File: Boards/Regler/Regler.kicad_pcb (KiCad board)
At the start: 2 copper layers, 160 x 50 mm, 6 parts, among them P1 LV_In, P2 LV_Out_L, P3 LV_Out_R

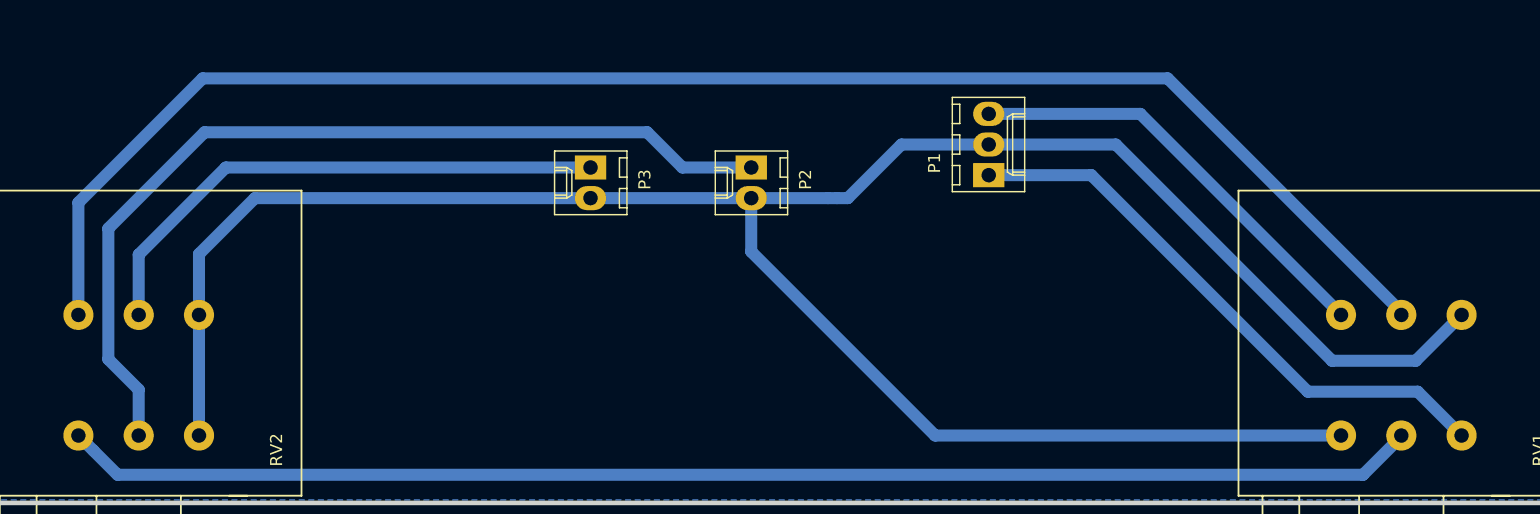
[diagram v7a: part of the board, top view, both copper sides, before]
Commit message: Added Test, moved mounting holes
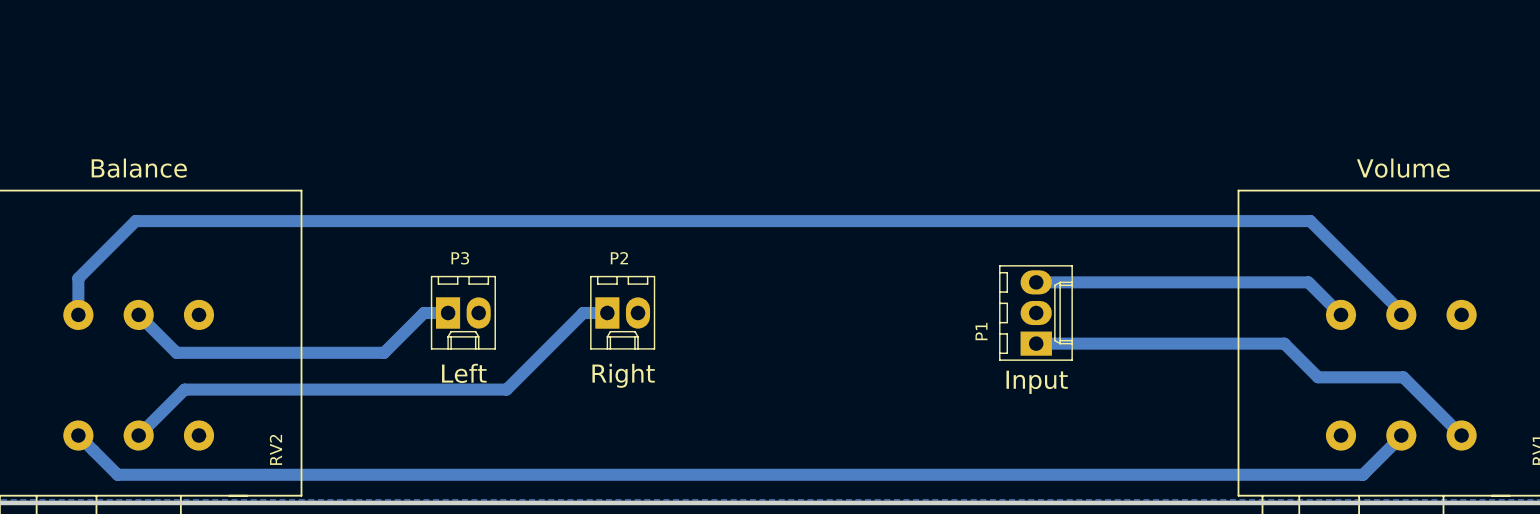
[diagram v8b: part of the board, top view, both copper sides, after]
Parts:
- moved P2 17.0 mm to (122.7, 121.9), turned to 0 degrees
- moved P3 16.9 mm to (109.5, 121.9), turned to 0 degrees
- moved P1 14.5 mm to (158.2, 124.5)
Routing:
- net Earth_Clean: track 192.2 -> 0.00 mm
- net Net-(P2-Pad1): track 76.0 -> 43.1 mm
- net Net-(P3-Pad1): track 45.5 -> 28.3 mm
- net Net-(RV1-Pad5): track 131.5 -> 118.1 mm
- net Net-(P1-Pad3): track 36.1 -> 26.4 mm
- net Net-(P1-Pad1): track 48.2 -> 38.4 mm
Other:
- board text added: "Balance"
- board text added: "Input"
- board text added: "Left"
- board text added: "Right"
- board text added: "Volume"
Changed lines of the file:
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@@
-(kicad_pcb (version 20171130) (host pcbnew "(5.1.0)-1")
+(kicad_pcb (version 20171130) (host pcbnew "(5.1.4)-1")
   (general
     (thickness 1.6)
-    (drawings 0)
-    (tracks 44)
+    (drawings 5)
+    (tracks 24)
     (zones 0)
     (modules 6)
@@
   )
   (module Connectors_Molex:Molex_KK-6410-03_03x2.54mm_Straight (layer F.Cu)
-    (at 154.305 110.49 90)
+    (at 158.242 124.46 90)
     (descr "Connector Headers with Friction Lock, 22-27-2031, http://www.molex.com/pdm_docs/sd/022272021_sd.pdf")
     (tags "connector molex kk_6410 22-27-2031")
@@
   )
   (module Connectors_Molex:Molex_KK-6410-02_02x2.54mm_Straight (layer F.Cu)
-    (at 134.60984 109.855 270)
+    (at 122.682 121.92)
     (descr "Connector Headers with Friction Lock, 22-27-2021, http://www.molex.com/pdm_docs/sd/022272021_sd.pdf")
     (tags "connector molex kk_6410 22-27-2021")
-    (fp_text reference P2 (at 1 -4.5 270) (layer F.SilkS)
-      (effects (font (size 1 1) (thickness 0.15)))
-    )
-    (fp_text value LV_Out_L (at 1.27 4.5 270) (layer F.Fab)
+    (fp_text reference P2 (at 1 -4.5 180) (layer F.SilkS)
+      (effects (font (size 1 1) (thickness 0.15)))
+    )
+    (fp_text value LV_Out_L (at 1.27 4.5 180) (layer F.Fab)
       (effects (font (size 1 1) (thickness 0.15)))
     )
@@
     (fp_line (start 4.45 -3.55) (end 4.45 3.5) (layer F.CrtYd) (width 0.05))
     (fp_line (start 4.45 3.5) (end -1.9 3.5) (layer F.CrtYd) (width 0.05))
-    (fp_text user %R (at 1.27 0 270) (layer F.Fab)
-      (effects (font (size 1 1) (thickness 0.15)))
-    )
-    (pad 1 thru_hole rect (at 0 0 270) (size 2 2.6) (drill 1.2) (layers *.Cu *.Mask)
+    (fp_text user %R (at 1.27 0 180) (layer F.Fab)
+      (effects (font (size 1 1) (thickness 0.15)))
+    )
+    (pad 1 thru_hole rect (at 0 0) (size 2 2.6) (drill 1.2) (layers *.Cu *.Mask)
       (net 6 "Net-(P2-Pad1)"))
-    (pad 2 thru_hole oval (at 2.54 0 270) (size 2 2.6) (drill 1.2) (layers *.Cu *.Mask)
+    (pad 2 thru_hole oval (at 2.54 0) (size 2 2.6) (drill 1.2) (layers *.Cu *.Mask)
       (net 1 Earth_Clean))
     (model ${KISYS3DMOD}/Connectors_Molex.3dshapes/Molex_KK-6410-02_02x2.54mm_Straight.wrl
@@
   )
   (module Connectors_Molex:Molex_KK-6410-02_02x2.54mm_Straight (layer F.Cu)
-    (at 121.285 109.855 270)
+    (at 109.474 121.92)
     (descr "Connector Headers with Friction Lock, 22-27-2021, http://www.molex.com/pdm_docs/sd/022272021_sd.pdf")
     (tags "connector molex kk_6410 22-27-2021")
-    (fp_text reference P3 (at 1 -4.5 270) (layer F.SilkS)
-      (effects (font (size 1 1) (thickness 0.15)))
-    )
-    (fp_text value LV_Out_R (at 1.27 4.5 270) (layer F.Fab)
+    (fp_text reference P3 (at 1 -4.5 180) (layer F.SilkS)
+      (effects (font (size 1 1) (thickness 0.15)))
+    )
+    (fp_text value LV_Out_R (at 1.27 4.5 180) (layer F.Fab)
       (effects (font (size 1 1) (thickness 0.15)))
     )
@@
     (fp_line (start 4.45 -3.55) (end 4.45 3.5) (layer F.CrtYd) (width 0.05))
     (fp_line (start 4.45 3.5) (end -1.9 3.5) (layer F.CrtYd) (width 0.05))
-    (fp_text user %R (at 1.27 0 270) (layer F.Fab)
-      (effects (font (size 1 1) (thickness 0.15)))
-    )
-    (pad 1 thru_hole rect (at 0 0 270) (size 2 2.6) (drill 1.2) (layers *.Cu *.Mask)
+    (fp_text user %R (at 1.27 0 180) (layer F.Fab)
+      (effects (font (size 1 1) (thickness 0.15)))
+    )
+    (pad 1 thru_hole rect (at 0 0) (size 2 2.6) (drill 1.2) (layers *.Cu *.Mask)
       (net 7 "Net-(P3-Pad1)"))
-    (pad 2 thru_hole oval (at 2.54 0 270) (size 2 2.6) (drill 1.2) (layers *.Cu *.Mask)
+    (pad 2 thru_hole oval (at 2.54 0) (size 2 2.6) (drill 1.2) (layers *.Cu *.Mask)
       (net 1 Earth_Clean))
     (model ${KISYS3DMOD}/Connectors_Molex.3dshapes/Molex_KK-6410-02_02x2.54mm_Straight.wrl
@@
     )
   )
-  (segment (start 140.97 112.395) (end 141.732 112.395) (width 1) (layer B.Cu) (net 1))
-  (segment (start 134.60984 112.395) (end 140.97 112.395) (width 1) (layer B.Cu) (net 1))
-  (segment (start 121.285 112.395) (end 134.60984 112.395) (width 1) (layer B.Cu) (net 1))
-  (segment (start 121.285 112.395) (end 93.460569 112.395) (width 1) (layer B.Cu) (net 1))
-  (segment (start 93.460569 112.395) (end 88.82 117.035569) (width 1) (layer B.Cu) (net 1))
-  (segment (start 88.82 117.035569) (end 88.82 122.08) (width 1) (layer B.Cu) (net 1))
-  (segment (start 88.82 132.08) (end 88.82 122.08) (width 1) (layer B.Cu) (net 1))
-  (segment (start 142.621 112.395) (end 141.732 112.395) (width 1) (layer B.Cu) (net 1))
-  (segment (start 154.305 107.95) (end 147.066 107.95) (width 1) (layer B.Cu) (net 1))
-  (segment (start 147.066 107.95) (end 142.621 112.395) (width 1) (layer B.Cu) (net 1))
-  (segment (start 134.60984 116.82984) (end 134.60984 112.395) (width 1) (layer B.Cu) (net 1))
-  (segment (start 183.515 132.08) (end 149.86 132.08) (width 1) (layer B.Cu) (net 1))
-  (segment (start 149.86 132.08) (end 134.60984 116.82984) (width 1) (layer B.Cu) (net 1))
-  (segment (start 164.846 107.95) (end 154.305 107.95) (width 1) (layer B.Cu) (net 1))
-  (segment (start 182.776768 125.880768) (end 164.846 107.95) (width 1) (layer B.Cu) (net 1))
-  (segment (start 193.515 122.08) (end 189.714232 125.880768) (width 1) (layer B.Cu) (net 1))
-  (segment (start 189.714232 125.880768) (end 182.776768 125.880768) (width 1) (layer B.Cu) (net 1))
-  (segment (start 78.82 112.768719) (end 78.82 122.08) (width 1) (layer B.Cu) (net 2))
-  (segment (start 89.122368 102.466351) (end 78.82 112.768719) (width 1) (layer B.Cu) (net 2))
-  (segment (start 169.141351 102.466351) (end 89.122368 102.466351) (width 1) (layer B.Cu) (net 2))
+  (gr_text Balance (at 83.82 109.982) (layer F.SilkS)
+    (effects (font (size 1.5 1.5) (thickness 0.3)))
+  )
+  (gr_text Volume (at 188.722 109.982) (layer F.SilkS)
+    (effects (font (size 1.5 1.5) (thickness 0.3)))
+  )
+  (gr_text Input (at 158.242 127.508) (layer F.SilkS)
+    (effects (font (size 1.5 1.5) (thickness 0.3)))
+  )
+  (gr_text Right (at 123.952 127) (layer F.SilkS)
+    (effects (font (size 1.5 1.5) (thickness 0.3)))
+  )
+  (gr_text Left (at 110.744 127) (layer F.SilkS)
+    (effects (font (size 1.5 1.5) (thickness 0.3)))
+  )
+  (segment (start 78.82 119.046) (end 78.82 122.08) (width 1) (layer B.Cu) (net 2))
+  (segment (start 83.566 114.3) (end 78.82 119.046) (width 1) (layer B.Cu) (net 2))
+  (segment (start 180.975 114.3) (end 83.566 114.3) (width 1) (layer B.Cu) (net 2))
   (segment (start 188.515 122.08) (end 188.515 121.84) (width 1) (layer B.Cu) (net 2))
-  (segment (start 188.515 121.84) (end 169.141351 102.466351) (width 1) (layer B.Cu) (net 2))
+  (segment (start 188.515 121.84) (end 180.975 114.3) (width 1) (layer B.Cu) (net 2))
   (segment (start 80.069679 133.329679) (end 78.82 132.08) (width 1) (layer B.Cu) (net 3))
   (segment (start 82.073896 135.333896) (end 80.069679 133.329679) (width 1) (layer B.Cu) (net 3))
@@
   (segment (start 188.515 132.08) (end 188.515 132.16) (width 1) (layer B.Cu) (net 3))
   (segment (start 188.515 132.16) (end 185.341104 135.333896) (width 1) (layer B.Cu) (net 3))
-  (segment (start 162.814 110.49) (end 154.305 110.49) (width 1) (layer B.Cu) (net 4))
-  (segment (start 180.768734 128.444734) (end 162.814 110.49) (width 1) (layer B.Cu) (net 4))
-  (segment (start 193.515 132.08) (end 189.879734 128.444734) (width 1) (layer B.Cu) (net 4))
-  (segment (start 189.879734 128.444734) (end 180.768734 128.444734) (width 1) (layer B.Cu) (net 4))
-  (segment (start 183.515 122.047) (end 183.515 122.08) (width 1) (layer B.Cu) (net 5))
-  (segment (start 154.305 105.41) (end 166.878 105.41) (width 1) (layer B.Cu) (net 5))
-  (segment (start 166.878 105.41) (end 183.515 122.047) (width 1) (layer B.Cu) (net 5))
-  (segment (start 128.905 109.855) (end 125.984963 106.934963) (width 1) (layer B.Cu) (net 6))
-  (segment (start 83.82 128.27) (end 83.82 132.08) (width 1) (layer B.Cu) (net 6))
-  (segment (start 134.60984 109.855) (end 128.905 109.855) (width 1) (layer B.Cu) (net 6))
-  (segment (start 125.984963 106.934963) (end 89.280037 106.934963) (width 1) (layer B.Cu) (net 6))
-  (segment (start 89.280037 106.934963) (end 81.30279 114.91221) (width 1) (layer B.Cu) (net 6))
-  (segment (start 81.30279 114.91221) (end 81.30279 125.75279) (width 1) (layer B.Cu) (net 6))
-  (segment (start 81.30279 125.75279) (end 83.82 128.27) (width 1) (layer B.Cu) (net 6))
-  (segment (start 91.045972 109.855) (end 83.82 117.080972) (width 1) (layer B.Cu) (net 7))
-  (segment (start 121.285 109.855) (end 91.045972 109.855) (width 1) (layer B.Cu) (net 7))
-  (segment (start 83.82 117.080972) (end 83.82 122.08) (width 1) (layer B.Cu) (net 7))
+  (segment (start 188.689 127.254) (end 193.515 132.08) (width 1) (layer B.Cu) (net 4))
+  (segment (start 181.61 127.254) (end 188.689 127.254) (width 1) (layer B.Cu) (net 4))
+  (segment (start 158.242 124.46) (end 178.816 124.46) (width 1) (layer B.Cu) (net 4))
+  (segment (start 178.816 124.46) (end 181.61 127.254) (width 1) (layer B.Cu) (net 4))
+  (segment (start 180.815 119.38) (end 183.515 122.08) (width 1) (layer B.Cu) (net 5))
+  (segment (start 158.242 119.38) (end 180.815 119.38) (width 1) (layer B.Cu) (net 5))
+  (segment (start 120.682 121.92) (end 114.332 128.27) (width 1) (layer B.Cu) (net 6))
+  (segment (start 122.682 121.92) (end 120.682 121.92) (width 1) (layer B.Cu) (net 6))
+  (segment (start 87.63 128.27) (end 83.82 132.08) (width 1) (layer B.Cu) (net 6))
+  (segment (start 114.332 128.27) (end 87.63 128.27) (width 1) (layer B.Cu) (net 6))
+  (segment (start 107.474 121.92) (end 104.172 125.222) (width 1) (layer B.Cu) (net 7))
+  (segment (start 109.474 121.92) (end 107.474 121.92) (width 1) (layer B.Cu) (net 7))
+  (segment (start 86.962 125.222) (end 83.82 122.08) (width 1) (layer B.Cu) (net 7))
+  (segment (start 104.172 125.222) (end 86.962 125.222) (width 1) (layer B.Cu) (net 7))
   (zone (net 1) (net_name Earth_Clean) (layer B.Cu) (hatch edge 0.508)
     (connect_pads (clearance 0.508))
